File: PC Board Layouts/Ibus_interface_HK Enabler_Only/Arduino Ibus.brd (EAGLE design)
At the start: 55.9 x 28.4 mm, 14 parts

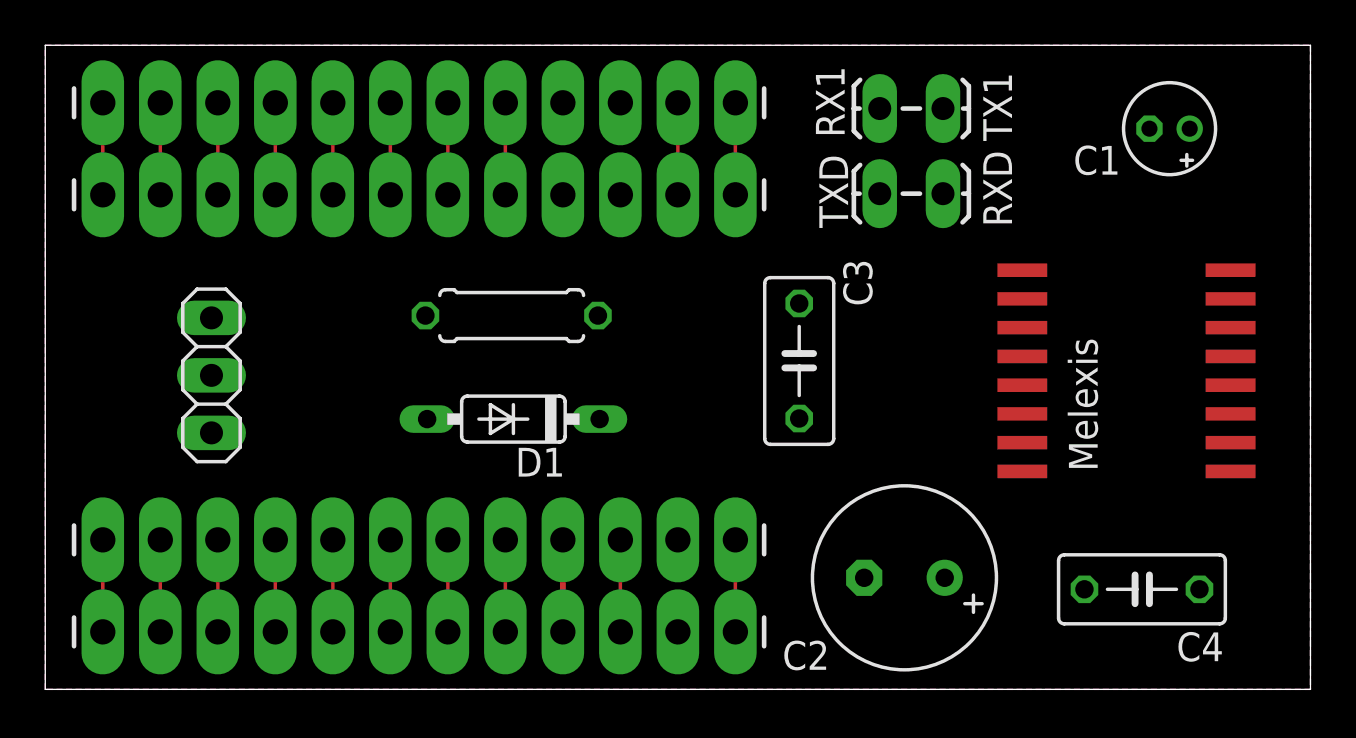
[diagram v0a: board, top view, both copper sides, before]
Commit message: Changed Brute Force PCB to be smaller with no options
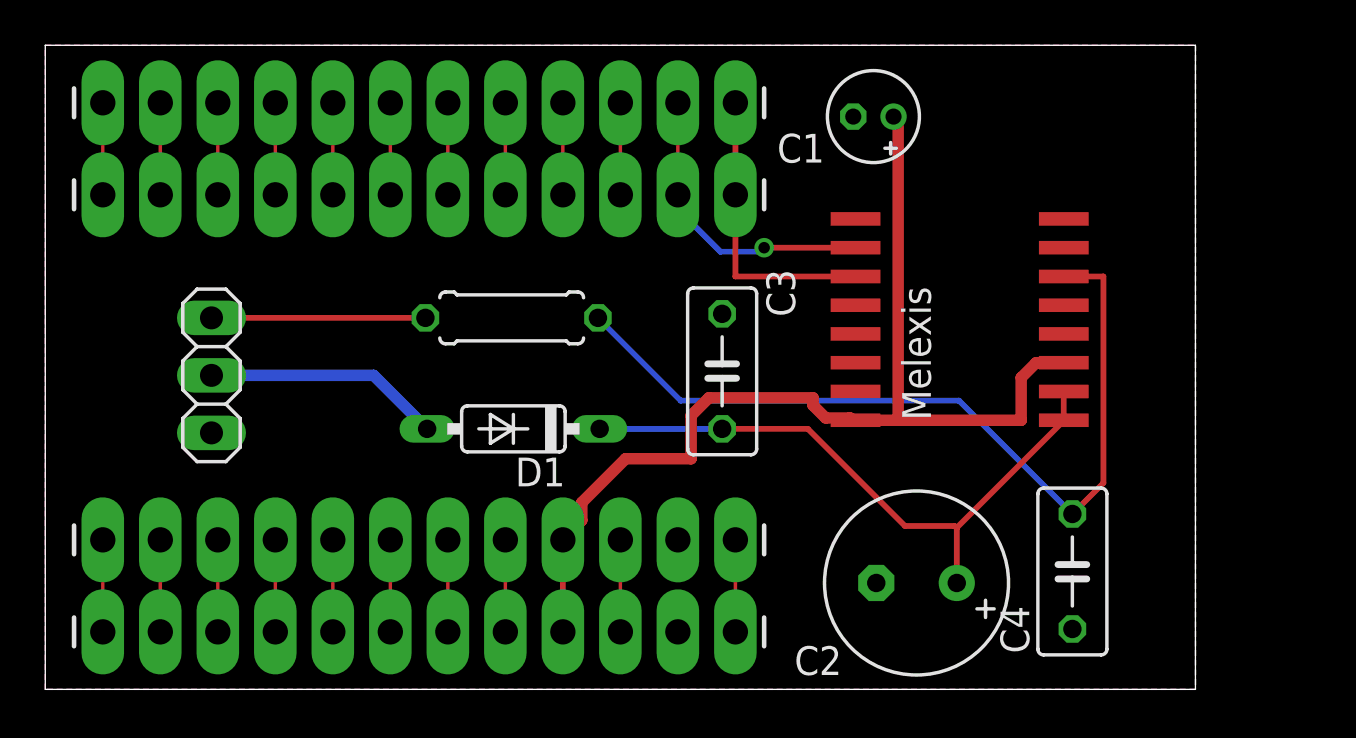
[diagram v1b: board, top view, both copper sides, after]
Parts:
- removed JP7, JP8: M02LOCK_LONGPADS, SparkFun-Connectors:1X02_LOCK_LONGPADS
- moved C1 13.1 mm to (36.6, 25.3)
- moved U$1 7.71 mm to (40.4, 16.3)
- moved C3 3.43 mm to (29.9, 14.0)
- moved C4 3.17 mm to (45.4, 5.21), turned to 270 degrees
- moved C2 0.58 mm to (38.5, 4.70)
- moved D1 0.43 mm to (20.7, 11.5)
- moved R1 0.10 mm to (20.6, 16.4)
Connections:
- removed net RXD: JP7.2, U$1.10
- removed net SENSE: U$1.15
- removed net TXD: JP7.1, U$1.11
- new net N$1: JP1.10, JP3.10
- new net N$2: JP1.9, JP3.9
- net D3: no longer U$1.9
- net D4: no longer U$1.14
- net GND: now also U$1.9; no longer JP1.10, JP1.9, JP3.10, JP3.9, U$1.7
- net RX1: now also U$1.10; no longer JP8.1
- net TX1: now also U$1.11; no longer JP8.2
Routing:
- net +5V: track 4.06 -> 46.6 mm
- net N$4: track 0.00 -> 37.4 mm
- net N$3: track 0.00 -> 28.0 mm
- net +12V: track 0.00 -> 10.5 mm
- net IBUS: track 0.00 -> 9.45 mm
- net RX1: track 4.06 -> 13.4 mm, vias 0 -> 1
- net TX1: track 4.06 -> 13.0 mm
- net N$2: track 0.00 -> 4.06 mm
- net N$1: track 0.00 -> 4.06 mm
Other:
- board size 55.9 x 28.4 mm -> 50.8 x 28.4 mm
- board text removed: "RX1"
- board text removed: "RXD"
- board text removed: "TX1"
- board text removed: "TXD"
